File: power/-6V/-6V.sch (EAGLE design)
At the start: 25 parts, among them U1 LM5575, X1 PINCON-1X4, X2 PINCON-1X4

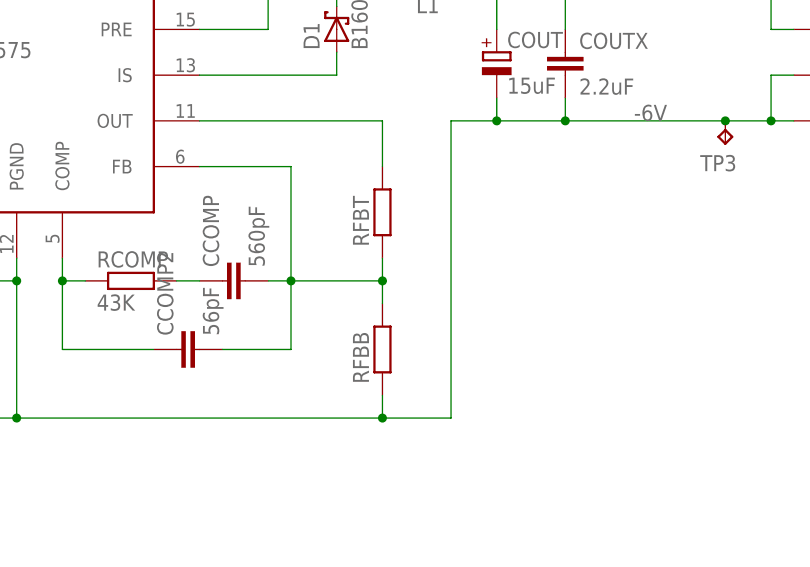
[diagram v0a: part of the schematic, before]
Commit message: added attributes to build a usable BOM
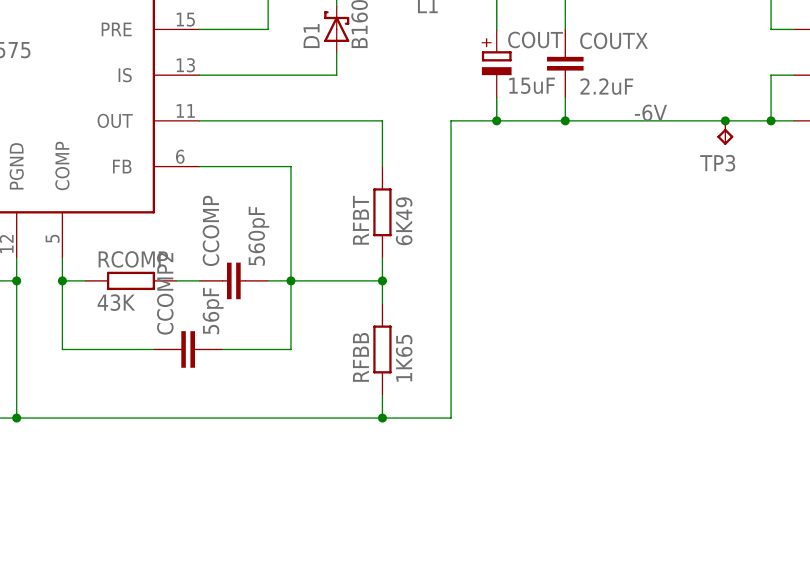
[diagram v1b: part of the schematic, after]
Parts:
- CIO: MANUFACTURER (none) -> TDK; MPN (none) -> C3216X7R1H105K; OC_DIGIKEY (none) -> 445-1423-1-ND; OC_FARNELL (none) -> 1907358; OC_MOUSER (none) -> 810-C3216X7R1H105K
- COUT: MANUFACTURER (none) -> Panasonic; MPN (none) -> 10SVP15M; OC_DIGIKEY (none) -> P16431CT-ND; OC_FARNELL (none) -> 9188886; OC_MOUSER (none) -> 667-10SVP15M
- COUTX: MANUFACTURER (none) -> Murata; MPN (none) -> GRM188R61A225KE34D; OC_DIGIKEY (none) -> 490-1545-1-ND; OC_FARNELL (none) -> 1828799; OC_MOUSER (none) -> 81-GRM188R61A225KE34
- L1: MANUFACTURER (none) -> Bourns; MPN (none) -> SDR1006-560KL; OC_DIGIKEY (none) -> SDR1006-560KLCT-ND; OC_FARNELL (none) -> 2309276; OC_MOUSER (none) -> 652-SDR1006-560KL
- RFBB: value (none) -> 1K65
- RFBT: value (none) -> 6K49
